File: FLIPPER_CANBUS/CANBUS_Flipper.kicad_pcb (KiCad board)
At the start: 2 copper layers, 67 x 21.3 mm, 31 parts, among them J1 Conn_01x08_Socket, J2 Conn_01x10_Socket, J3 Conn_01x02, J4 Conn_01x02_Socket, U1 MCP2515-xST, U2 MAX3051, Y1 16 Mhz

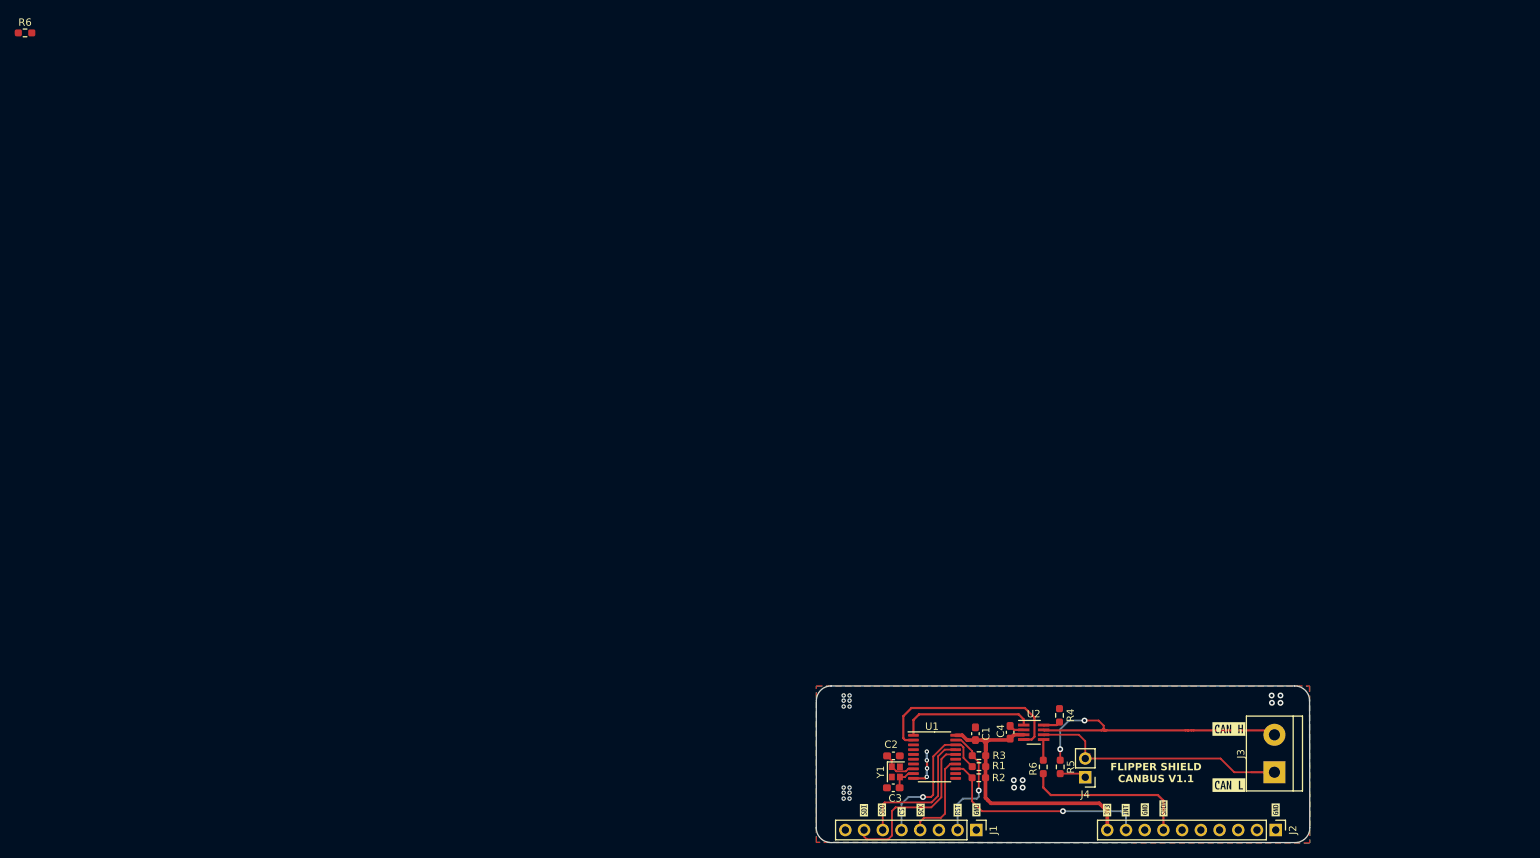
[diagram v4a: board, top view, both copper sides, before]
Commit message: feat(hw): Paths and jumper update
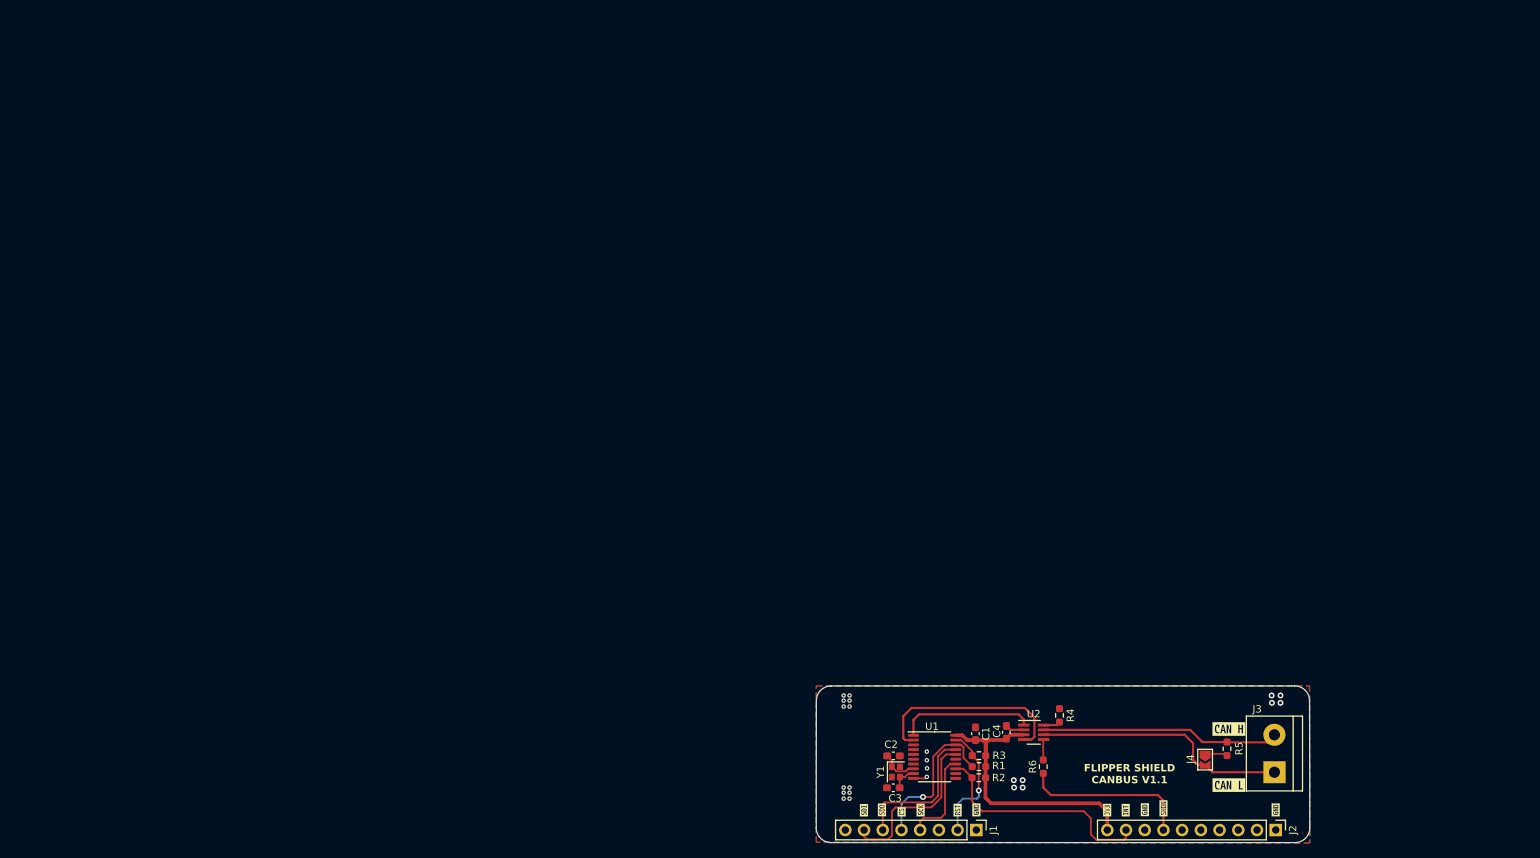
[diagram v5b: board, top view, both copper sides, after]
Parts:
- removed the R6 at (1.68, 0.76)
- removed the R6 at (139.9, 100.4)
- added R6: 0, Resistor_SMD:R_0603_1608Metric_Pad0.98x0.95mm_HandSolder, F.Cu at (139.9, 100.4)
- J4: footprint Connector_PinHeader_2.54mm:PinHeader_1x02_P2.54mm_Vertical -> Jumper:SolderJumper-2_P1.3mm_Open_TrianglePad1.0x1.5mm
- moved R5 22.8 mm to (164.8, 97.9)
- moved J4 16.4 mm to (161.9, 99.4), turned to -90 degrees
- moved C4 0.51 mm to (134.9, 95.7)
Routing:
- net /CANH: track 43.8 -> 33.5 mm, vias 2 -> 0
- net GND: track 7.42 -> 4.56 mm
- net /INT: track 29.7 -> 31.4 mm, vias 1 -> 0
- net /CANL: track 35.8 -> 34.8 mm
- net Net-(J4-Pin_1): track 3.60 -> 3.09 mm

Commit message: feat(hw): update design
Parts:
- moved C1 1.86 mm to (132.1, 94.7)
- moved R3 1.66 mm to (131.2, 97.2)
- moved R1 1.31 mm to (131.2, 99.0)
- moved R2 1.13 mm to (131.2, 100.7)
- moved C2 0.84 mm to (119.5, 98.1)
- moved C4 0.63 mm to (135.0, 95.1)
- moved Y1 0.48 mm to (119.9, 100.6)
- moved C3 0.35 mm to (119.5, 102.9)
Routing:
- net /RXD: track 27.5 -> 30.8 mm
- net /TXD: track 18.4 -> 20.8 mm
- net GND: track 4.56 -> 6.50 mm
- net /INT: track 31.4 -> 32.1 mm
- net /RST: track 16.2 -> 16.9 mm
- net +3.3V: track 39.3 -> 38.7 mm
- net /CS: track 21.6 -> 21.0 mm

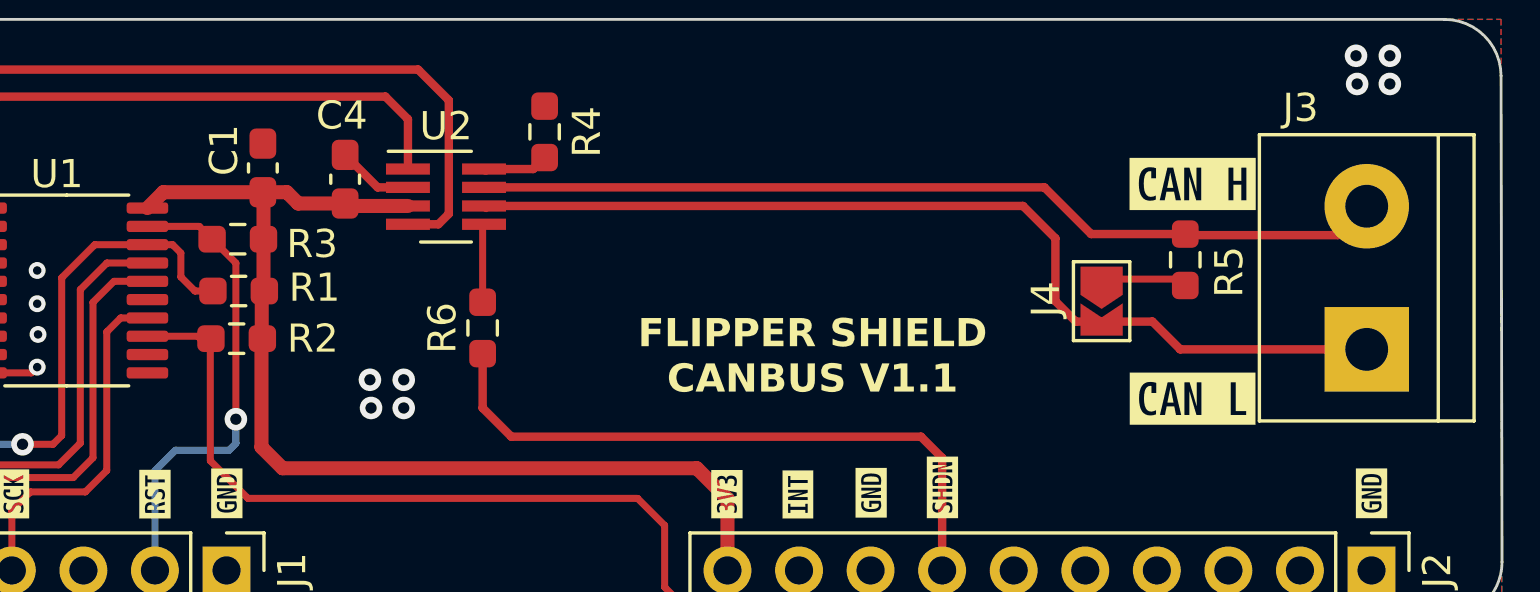
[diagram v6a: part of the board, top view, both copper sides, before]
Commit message: feat(hw): jumper changed and bom added
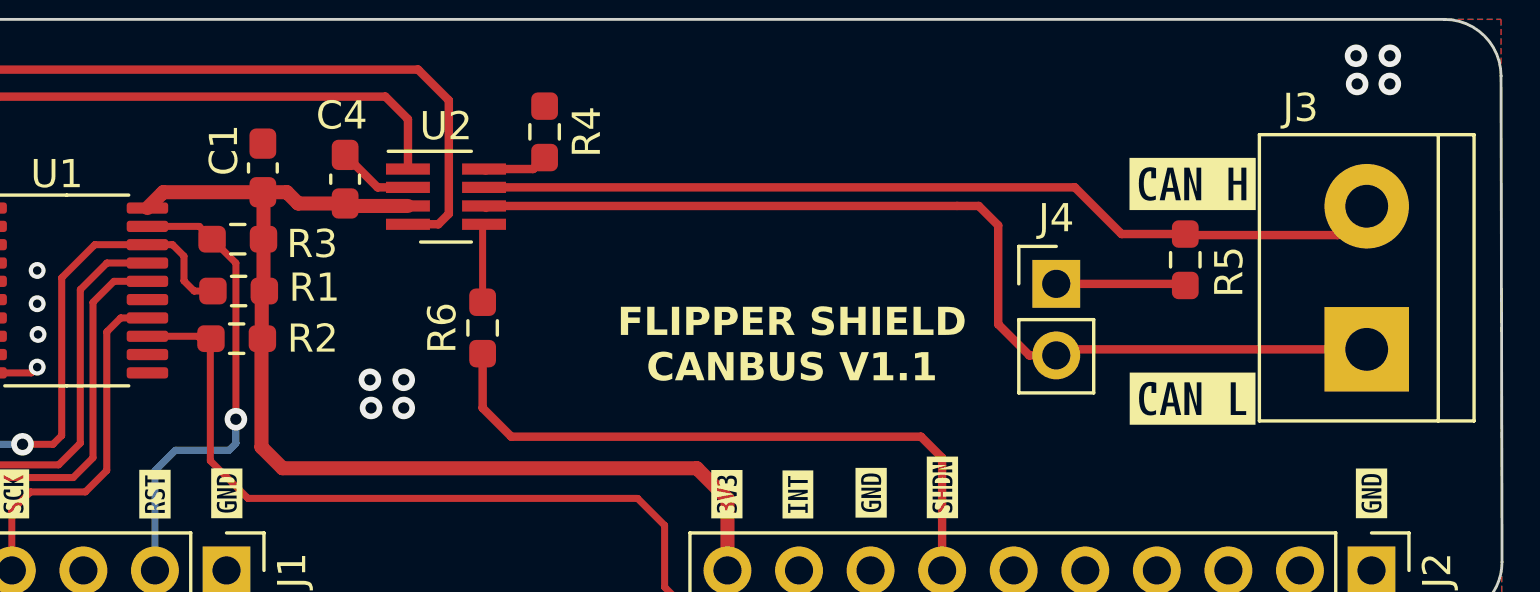
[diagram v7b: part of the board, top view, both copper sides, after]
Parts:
- J4: footprint Jumper:SolderJumper-2_P1.3mm_Open_TrianglePad1.0x1.5mm -> Connector_PinHeader_2.54mm:PinHeader_1x02_P2.54mm_Vertical
- moved J4 1.72 mm to (160.3, 98.8), turned to 0 degrees
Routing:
- net Net-(J4-Pin_1): track 3.09 -> 4.60 mm
- net /CANL: track 34.8 -> 35.8 mm

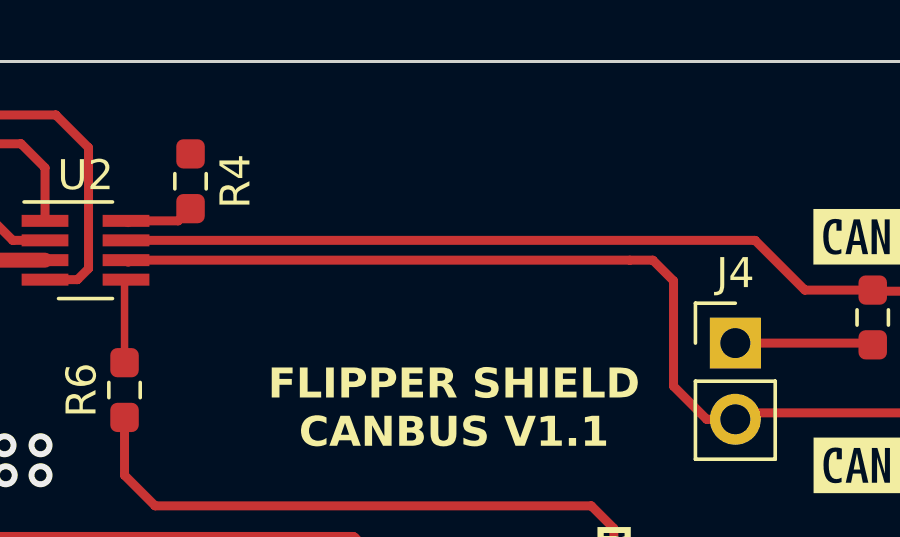
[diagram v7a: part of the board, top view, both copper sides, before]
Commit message: feat(hw): add logo and Kicad8
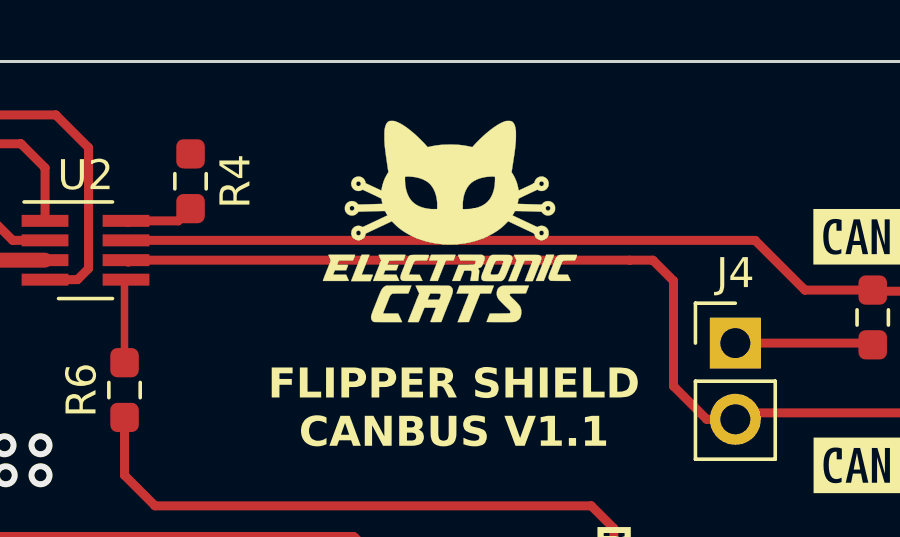
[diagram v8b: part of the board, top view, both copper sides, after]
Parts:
- added G***: LOGO, Aesthetics:electronic_cats_logo_8x6, F.Cu at (150.7, 94.7)
- added G***: LOGO, Aesthetics:electronic_cats_logo_8x6, B.Cu at (150.6, 94.9)
- added REF**: OSHW-Logo2_9.8x8mm_SilkScreen, Symbol:OSHW-Logo2_9.8x8mm_SilkScreen, B.Cu at (126.4, 94.6)
